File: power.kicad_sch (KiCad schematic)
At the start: 9 parts

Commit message: feat: final quick fixes
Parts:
- LP1: footprint Inductor_SMD:L_7.3x7.3_H4.5 -> Inductor_SMD:L_12x12mm_H4.5mm
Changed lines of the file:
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@@
 			)
 		)
-		(property "Footprint" "Inductor_SMD:L_7.3x7.3_H4.5"
+		(property "Footprint" "Inductor_SMD:L_12x12mm_H4.5mm"
 			(at 232.41 102.87 0)
 			(effects

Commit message: tarjeta para raspberri, pdfs y relacion de pines
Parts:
- DP3: footprint Diode_SMD:D_SMB_Handsoldering -> Diode_THT:D_DO-41_SOD81_P10.16mm_Horizontal
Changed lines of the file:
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@@
 			)
 		)
-		(property "Footprint" "Diode_SMD:D_SMB_Handsoldering"
+		(property "Footprint" "Diode_THT:D_DO-41_SOD81_P10.16mm_Horizontal"
 			(at 153.035 102.87 0)
 			(effects

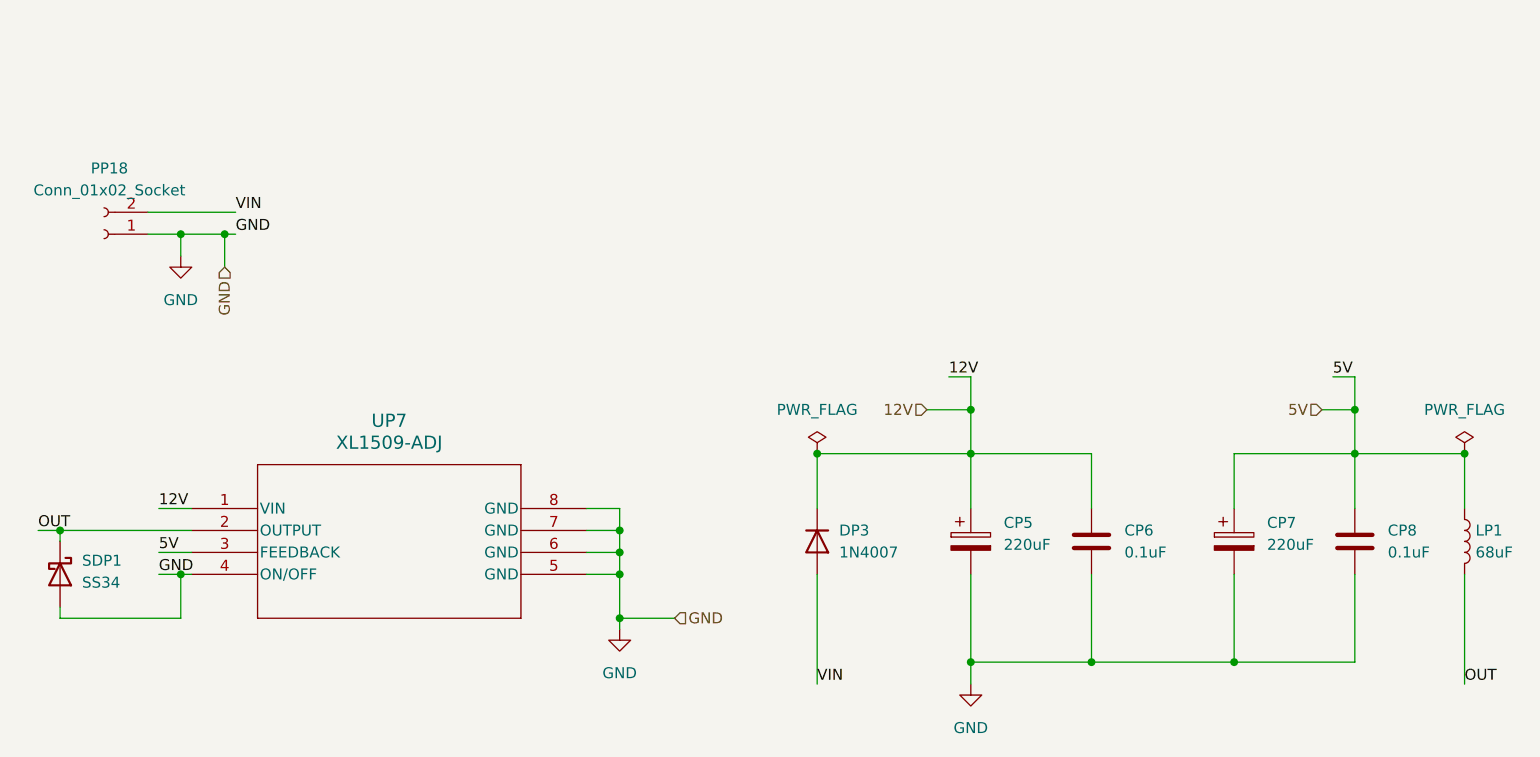
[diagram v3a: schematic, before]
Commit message: en proceso de hacer el diseño, coloque el modulo de adc a i2c por que es mas barato que comprar las piezas
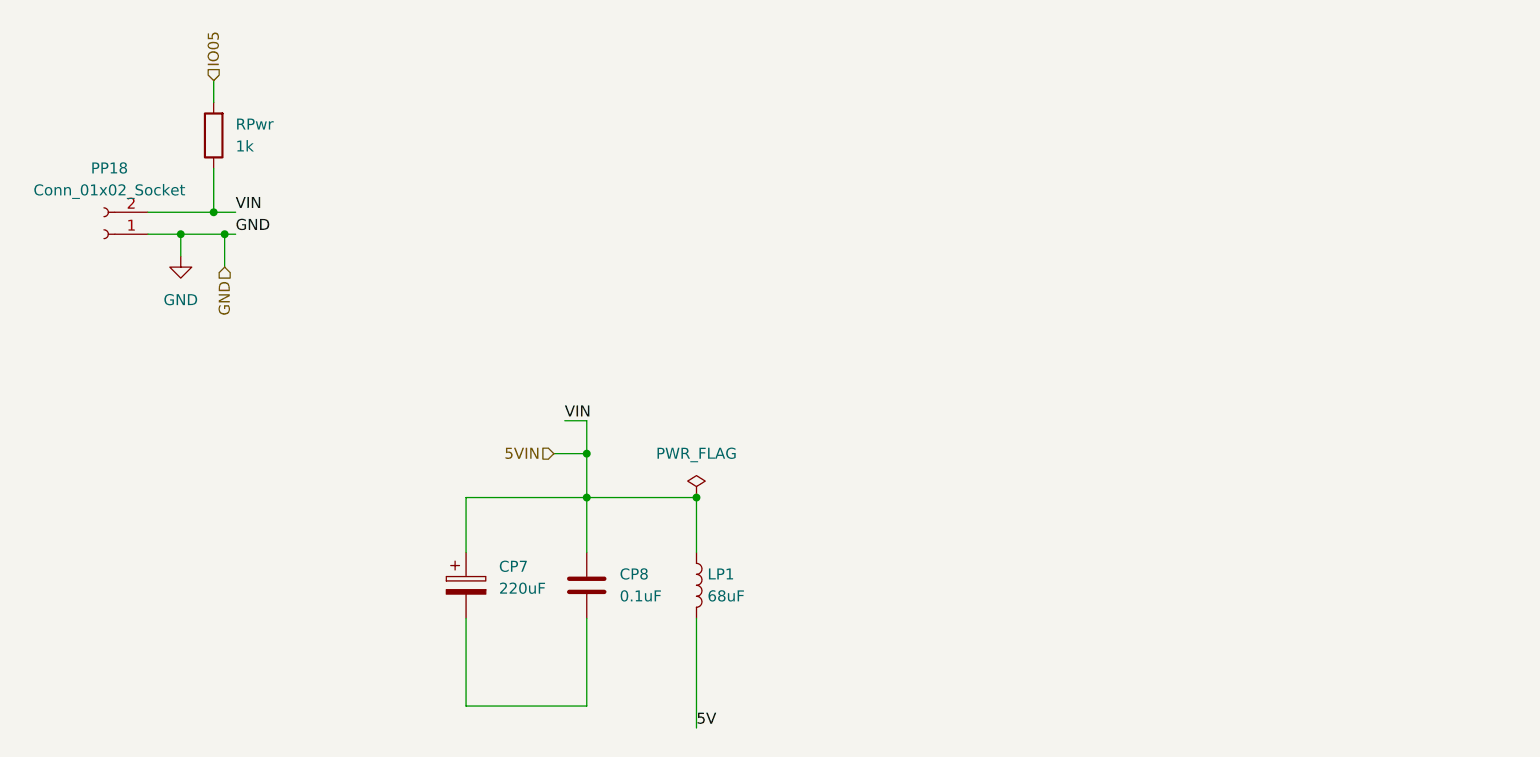
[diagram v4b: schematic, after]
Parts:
- removed CP5: 220uF, Capacitor_THT:CP_Radial_D8.0mm_P3.50mm, symbol Device:C_Polarized
- removed CP6: 0.1uF, Capacitor_SMD:C_1206_3216Metric, symbol Device:C
- removed DP3: 1N4007, Diode_THT:D_DO-41_SOD81_P10.16mm_Horizontal, symbol Diode:1N4007
- removed SDP1: SS34, Diode_SMD:D_SMA, symbol Diode:SS34
- removed UP7: XL1509-ADJ, SOIC-8_YTS, symbol Xl_1509_5.0:XL1509-ADJ
- added RPwr: 1k, Resistor_SMD:R_1206_3216Metric_Pad1.30x1.75mm_HandSolder, symbol Device:R
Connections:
- net OUT is gone; now on net 5V: LP1.2
- net 5V: no longer CP7.1, CP8.1, LP1.1
- net GND: no longer CP7.2, CP8.2
- net VIN renamed 5VIN
- net 5VIN: now also CP7.1, CP8.1, LP1.1, RPwr.1
- new net: CP7.2, CP8.2
- new net IO05: RPwr.2
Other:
- moved on the sheet: CP7, CP8, LP1
